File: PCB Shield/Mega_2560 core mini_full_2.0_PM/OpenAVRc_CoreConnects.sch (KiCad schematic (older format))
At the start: 15 parts, among them P1 2560-core, P10 RX1TX1, P16 LCD, P6 Micro_sd, P9 SPI

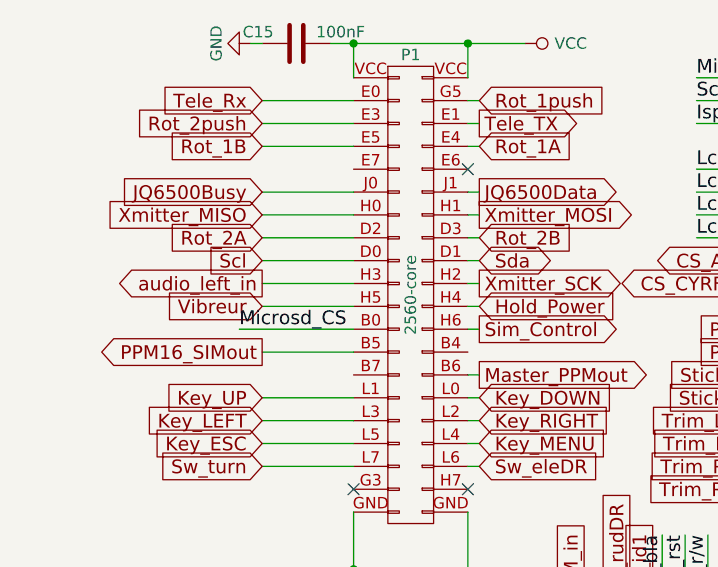
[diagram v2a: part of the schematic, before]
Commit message: Some changes on schematic's shield (JQ and haptic labels)
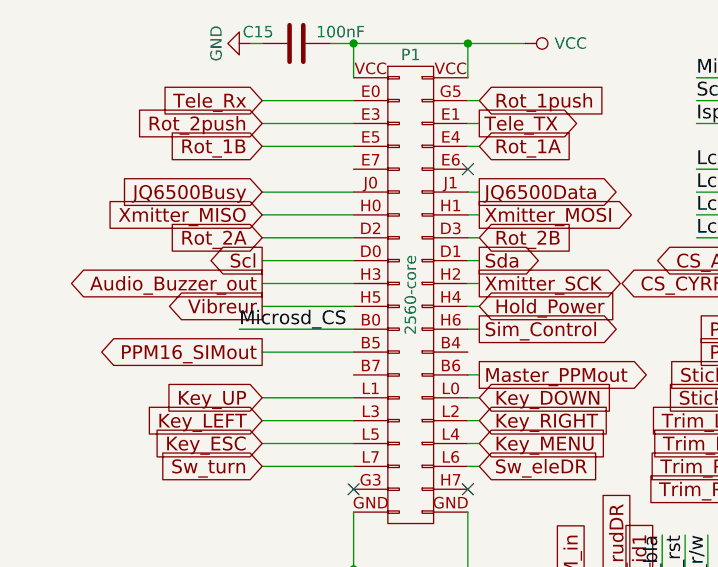
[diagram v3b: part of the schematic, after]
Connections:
- net audio_left_in renamed Audio_Buzzer_out
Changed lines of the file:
@@
 Text GLabel 1450 2950 0    60   Input ~ 0
 Rot_2A
-Text GLabel 1450 3050 0    60   Input ~ 0
+Text GLabel 1450 3050 0    60   Output ~ 0
 Scl
 Text GLabel 1450 3150 0    60   Output ~ 0
-audio_left_in
-Text GLabel 1450 3250 0    60   Input ~ 0
-Vibreur
+Audio_Buzzer_out
 Text GLabel 1450 3650 0    60   Input ~ 0
 Key_UP
@@
 Text GLabel 2400 2950 2    60   Input ~ 0
 Rot_2B
-Text GLabel 2400 3050 2    60   BiDi ~ 0
+Text GLabel 2400 3050 2    60   Output ~ 0
 Sda
 Text GLabel 2400 3150 2    60   Output ~ 0
@@
 Wire Wire Line
 	8850 2150 8850 2250
+Text GLabel 1450 3250 0    60   Output ~ 0
+Vibreur
 $EndSCHEMATC

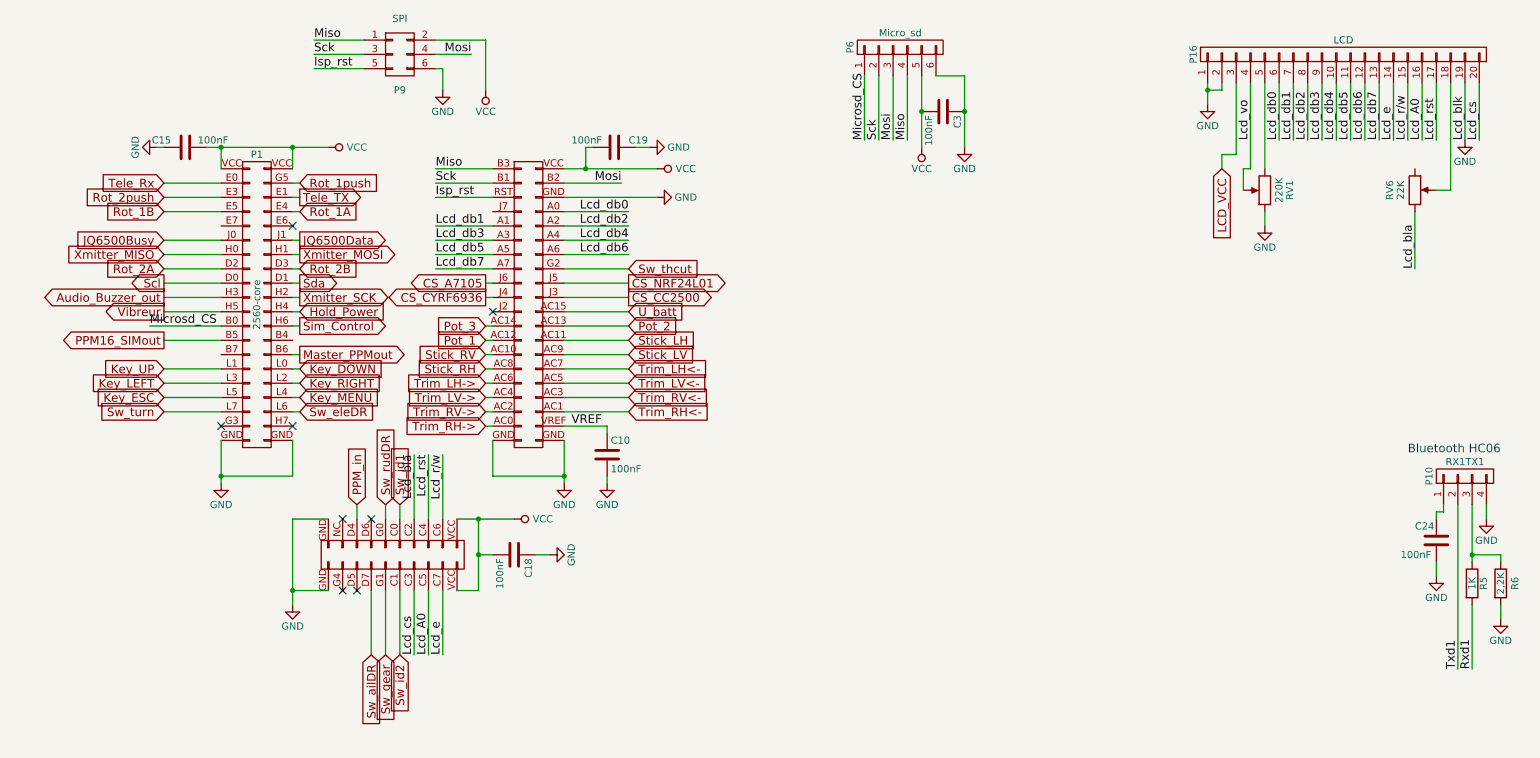
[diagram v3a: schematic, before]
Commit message: Update schematic sheets
Move Rot_2A on E7 and Rot2A on E6
Add BT_txd1 on D3 and BT_rxd1 on D2
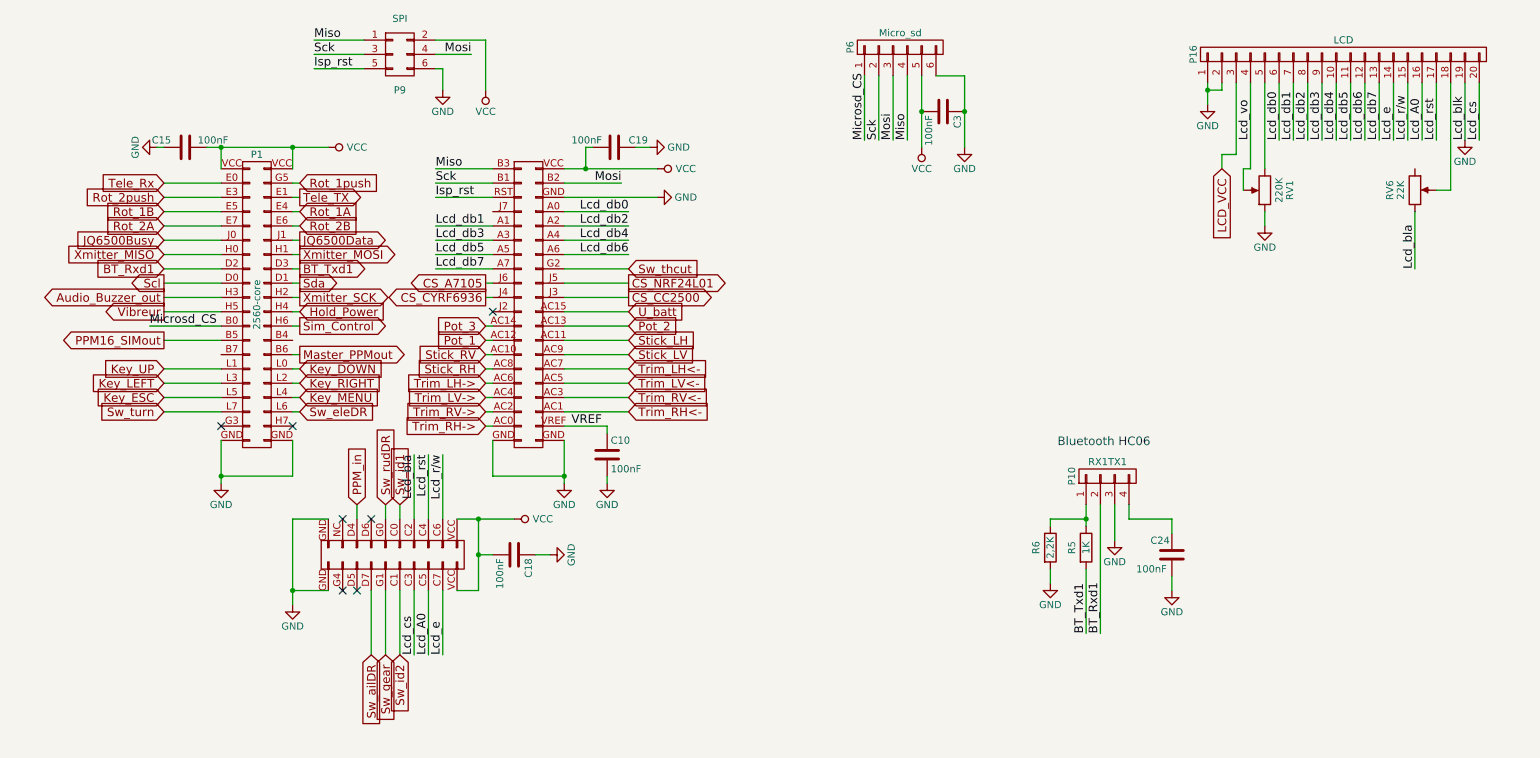
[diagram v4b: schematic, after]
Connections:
- net GND: now also P10.3 (P3); no longer P10.4 (P4)
- net Rot_2A: now also P1.E7 (P10); no longer P1.D2 (P16)
- net Rot_2B: now also P1.E6 (P9); no longer P1.D3 (P15)
- net at P10.1 (P1): now also R5.1, R6.1; no longer C24.1
- net Rxd1 renamed BT_Txd1
- net BT_Txd1: now also P1.D3 (P15)
- net Txd1 renamed BT_Rxd1
- net BT_Rxd1: now also P1.D2 (P16)
- new net: C24.1, P10.4 (P4)
- no-connect marks 8 -> 7
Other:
- moved on the sheet: C24, P10, R5, R6

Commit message: Update schematic and pcb
Add PM-5033 as other dc/dc option
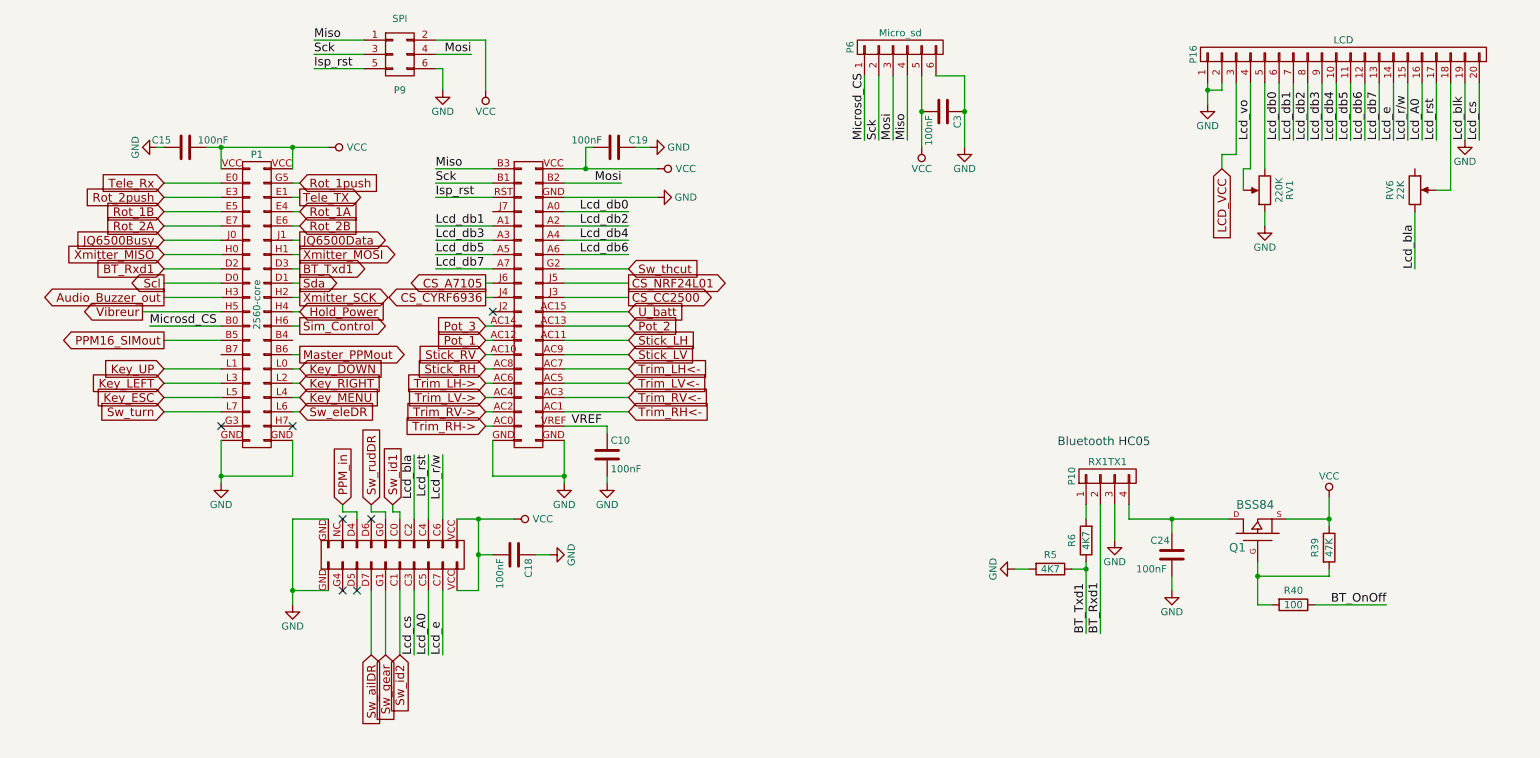
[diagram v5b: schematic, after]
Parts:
- added Q1: BSS84, symbol MOSFET_P
- added R39: 47K, Resistors_SMD:R_1206, symbol R-RESCUE-Mega_2560_core_mini_full_2.0
- added R40: 100, Resistors_SMD:R_1206, symbol R-RESCUE-Mega_2560_core_mini_full_2.0
- R5: value 1K -> 4K7
- R6: value 2,2K -> 4K7
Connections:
- net BT_Txd1: now also R5.1, R6.1; no longer R5.2
- net GND: now also R5.2; no longer R6.2
- net VCC: now also Q1.S, R39.1
- net at C24.1, P10.4 (P4): now also Q1.D
- new net: P10.1 (P1), R6.2
- new net: Q1.G, R39.2, R40.2
- new net BT_OnOff: R40.1
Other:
- note added: "Bluetooth HC05"
- note removed: "Bluetooth HC06"
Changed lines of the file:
@@
 Sheet 3 7
 Title "Shield Mega2560 core Full"
-Date "2017-10-12"
+Date "2017-11-05"
 Rev "2.00"
 Comp ""
@@
 BT_Txd1
 Text Notes 7700 4200 0    60   ~ 0
-Bluetooth HC06
-$Comp
-L R-RESCUE-Mega_2560_core_mini_full_2.0 R5
-U 1 1 59C5BEB7
-P 7900 4900
-F 0 "R5" V 7800 4900 50  0000 C CNN
-F 1 "1K" V 7900 4900 50  0000 C CNN
-F 2 "Resistors_SMD:R_1206" V 7830 4900 50  0001 C CNN
-F 3 "" H 7900 4900 50  0000 C CNN
-	1    7900 4900
-	1    0    0    -1
-$EndComp
-$Comp
-L R-RESCUE-Mega_2560_core_mini_full_2.0 R6
-U 1 1 59C5BEBE
-P 7650 4900
-F 0 "R6" V 7550 4900 50  0000 C CNN
-F 1 "2,2K" V 7650 4900 50  0000 C CNN
-F 2 "Resistors_SMD:R_1206" V 7580 4900 50  0001 C CNN
-F 3 "" H 7650 4900 50  0000 C CNN
-	1    7650 4900
-	1    0    0    -1
-$EndComp
-$Comp
-L GND-RESCUE-Mega_2560_core_mini_full_2.0 #PWR067
-U 1 1 59C5BEC5
-P 7650 5150
-F 0 "#PWR067" H 7650 4900 50  0001 C CNN
-F 1 "GND" H 7650 5000 50  0000 C CNN
-F 2 "" H 7650 5150 50  0000 C CNN
-F 3 "" H 7650 5150 50  0000 C CNN
-	1    7650 5150
-	1    0    0    -1
-$EndComp
+Bluetooth HC05
 Text GLabel 1450 2350 0    60   Input ~ 0
 Tele_Rx
@@
 Text GLabel 4700 3950 2    60   Input ~ 0
 Trim_RH<-
-Text GLabel 2800 4600 1    60   Input ~ 0
+Text GLabel 2700 4600 1    60   Input ~ 0
 PPM_in
-Text GLabel 3000 4600 1    60   Input ~ 0
+Text GLabel 2900 4600 1    60   Input ~ 0
 Sw_rudDR
-Text GLabel 3100 4600 1    60   Input ~ 0
+Text GLabel 3050 4600 1    60   Input ~ 0
 Sw_id1
 Text GLabel 2900 5650 3    60   Input ~ 0
@@
 Text GLabel 8850 2250 3    60   Input ~ 0
 LCD_VCC
-Text GLabel 1450 3250 0    60   Output ~ 0
+Text GLabel 1300 3250 0    60   Output ~ 0
 Vibreur
 Text GLabel 1450 2950 0    60   Input ~ 0
@@
 	8750 1650 8750 1800
 Wire Wire Line
-	7650 5050 7650 5150
-Connection ~ 7900 4700
-Wire Wire Line
-	7650 4700 7900 4700
-Wire Wire Line
-	7900 4600 7900 4750
-Wire Wire Line
-	7900 5050 7900 5500
-Wire Wire Line
 	8000 4600 8000 5500
 Wire Wire Line
@@
 	2400 3350 2350 3350
 Wire Wire Line
-	1850 3250 1450 3250
+	1300 3250 1850 3250
 Wire Wire Line
 	2350 3250 2400 3250
@@
 	1850 2750 1450 2750
 Wire Wire Line
-	2800 4700 2800 4600
+	2800 4700 2800 4650
+Wire Wire Line
+	2700 4650 2700 4600
 Wire Wire Line
 	4250 3150 4700 3150
@@
 Wire Wire Line
 	1350 3350 1850 3350
-Wire Wire Line
-	3000 4700 3000 4600
-Wire Wire Line
-	3100 4600 3100 4700
 Wire Wire Line
 	3200 4250 3200 4700
@@
 	8500 4700 8500 4800
 Wire Wire Line
-	8200 4700 8500 4700
+	8200 4700 8900 4700
 Wire Wire Line
 	8200 4700 8200 4600
 Wire Wire Line
-	7650 4750 7650 4700
-Wire Wire Line
 	2400 2650 2350 2650
+Connection ~ 8500 4700
+$Comp
+L R-RESCUE-Mega_2560_core_mini_full_2.0 R39
+U 1 1 59E0D037
+P 9600 4900
+F 0 "R39" V 9500 4900 50  0000 C CNN
+F 1 "47K" V 9600 4900 50  0000 C CNN
+F 2 "Resistors_SMD:R_1206" V 9530 4900 50  0001 C CNN
+F 3 "" H 9600 4900 50  0000 C CNN
+	1    9600 4900
+	1    0    0    -1
+$EndComp
+$Comp
+L MOSFET_P Q1
+U 1 1 59E0D99E
+P 9100 4800
+F 0 "Q1" V 9000 5000 60  0000 R CNN
+F 1 "BSS84" V 9300 4950 60  0000 R CNN
+F 2 "" H 9100 4800 60  0000 C CNN
+F 3 "" H 9100 4800 60  0000 C CNN
+	1    9100 4800
+	0    -1   -1   0
+$EndComp
+$Comp
+L VCC #PWR067
+U 1 1 59E0DFF9
+P 9600 4550
+F 0 "#PWR067" H 9600 4400 50  0001 C CNN
+F 1 "VCC" H 9600 4700 50  0000 C CNN
+F 2 "" H 9600 4550 50  0000 C CNN
+F 3 "" H 9600 4550 50  0000 C CNN
+	1    9600 4550
+	1    0    0    -1
+$EndComp
+Wire Wire Line
+	9300 4700 9600 4700
+Wire Wire Line
+	9600 4550 9600 4750
+Wire Wire Line
+	9600 5050 9600 5100
+Wire Wire Line
+	9600 5100 9100 5100
+Connection ~ 9600 4700
+Wire Wire Line
+	9500 5300 10000 5300
+Connection ~ 9100 5100
+Text Label 10000 5300 2    60   ~ 0
+BT_OnOff
+$Comp
+L R-RESCUE-Mega_2560_core_mini_full_2.0 R40
+U 1 1 59E0E920
+P 9350 5300
+F 0 "R40" V 9250 5300 50  0000 C CNN
+F 1 "100" V 9350 5300 50  0000 C CNN
+F 2 "Resistors_SMD:R_1206" V 9280 5300 50  0001 C CNN
+F 3 "" H 9350 5300 50  0000 C CNN
+	1    9350 5300
+	0    1    1    0
+$EndComp
+Wire Wire Line
+	9100 5300 9200 5300
+Wire Wire Line
+	9100 5000 9100 5300
+Wire Wire Line
+	2800 4650 2700 4650
+Wire Wire Line
+	3000 4650 2900 4650
+Wire Wire Line
+	2900 4650 2900 4600
+Wire Wire Line
+	3000 4700 3000 4650
+Wire Wire Line
+	3100 4700 3100 4650
+Wire Wire Line
+	3100 4650 3050 4650
+Wire Wire Line
+	3050 4650 3050 4600
+$Comp
+L R-RESCUE-Mega_2560_core_mini_full_2.0 R5
+U 1 1 59EF4793
+P 7650 5050
+F 0 "R5" V 7550 5050 50  0000 C CNN
+F 1 "4K7" V 7650 5050 50  0000 C CNN
+F 2 "Resistors_SMD:R_1206" V 7580 5050 50  0001 C CNN
+F 3 "" H 7650 5050 50  0000 C CNN
+	1    7650 5050
+	0    1    1    0
+$EndComp
+$Comp
+L R-RESCUE-Mega_2560_core_mini_full_2.0 R6
+U 1 1 59EF4881
+P 7900 4850
+F 0 "R6" V 8000 4850 50  0000 C CNN
+F 1 "4K7" V 7900 4850 50  0000 C CNN
+F 2 "Resistors_SMD:R_1206" V 7830 4850 50  0001 C CNN
+F 3 "" H 7900 4850 50  0000 C CNN
+	1    7900 4850
+	-1   0    0    1
+$EndComp
+Wire Wire Line
+	7900 5500 7900 5000
+Wire Wire Line
+	7900 4700 7900 4600
+Wire Wire Line
+	7800 5050 7900 5050
+Connection ~ 7900 5050
+Wire Wire Line
+	7500 5050 7400 5050
+$Comp
+L GND-RESCUE-Mega_2560_core_mini_full_2.0 #PWR068
+U 1 1 59EF4C7A
+P 7400 5050
+F 0 "#PWR068" H 7400 4800 50  0001 C CNN
+F 1 "GND" H 7400 4900 50  0000 C CNN
+F 2 "" H 7400 5050 50  0000 C CNN
+F 3 "" H 7400 5050 50  0000 C CNN
+	1    7400 5050
+	0    1    1    0
+$EndComp
 $EndSCHEMATC
